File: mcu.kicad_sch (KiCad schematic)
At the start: 15 parts, among them U1 RP2040, U2 W25Q128JVS, Y1 Crystal_GND24

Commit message: add 3d models and do other stuff
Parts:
- added R8, R9: 5.1k, Resistor_SMD:R_0402_1005Metric, symbol Device:R_Small
- C1, C2: footprint (none) -> Capacitor_SMD:C_0402_1005Metric
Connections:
- net +3V3: now also R8.2, R9.2
- net MOSI: now reaches U1.12 (GPIO9)
- net MISO: now reaches U1.13 (GPIO10)
- net SCK: now reaches U1.14 (GPIO11)
- net M_LED_D: now reaches U1.15 (GPIO12)
- net BARO_CS: now reaches U1.16 (GPIO13)
- net IMU_CS: now reaches U1.17 (GPIO14)
- net RADIO_CS: now reaches U1.2 (GPIO0)
- net M_S6: now reaches U1.27 (GPIO16)
- net M_S5: now reaches U1.28 (GPIO17)
- net RADIO_D0: now reaches U1.3 (GPIO1)
- net M_S4: now reaches U1.36 (GPIO24)
- net M_S3: now reaches U1.37 (GPIO25)
- net BATTERY_SENSE: now reaches U1.38 (GPIO26_ADC0)
- net RADIO_RESET: now reaches U1.4 (GPIO2)
- net M_S1: now reaches U1.40 (GPIO28_ADC2)
- net M_S2: now reaches U1.41 (GPIO29_ADC3)
- net SDA: now reaches U1.6 (GPIO4)
- net SDA: now also R8.1
- net SCL: now reaches U1.7 (GPIO5)
- net SCL: now also R9.1
- net ARM_SWITCH: now reaches U1.8 (GPIO6)

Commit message: add some TVS diodes
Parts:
- added C25: 100n, Capacitor_SMD:C_0402_1005Metric, symbol Device:C_Small
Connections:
- net +3V3: now also U2.8 (VCC), C25.1
- net GND: now also C25.2
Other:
- moved on the sheet: U2

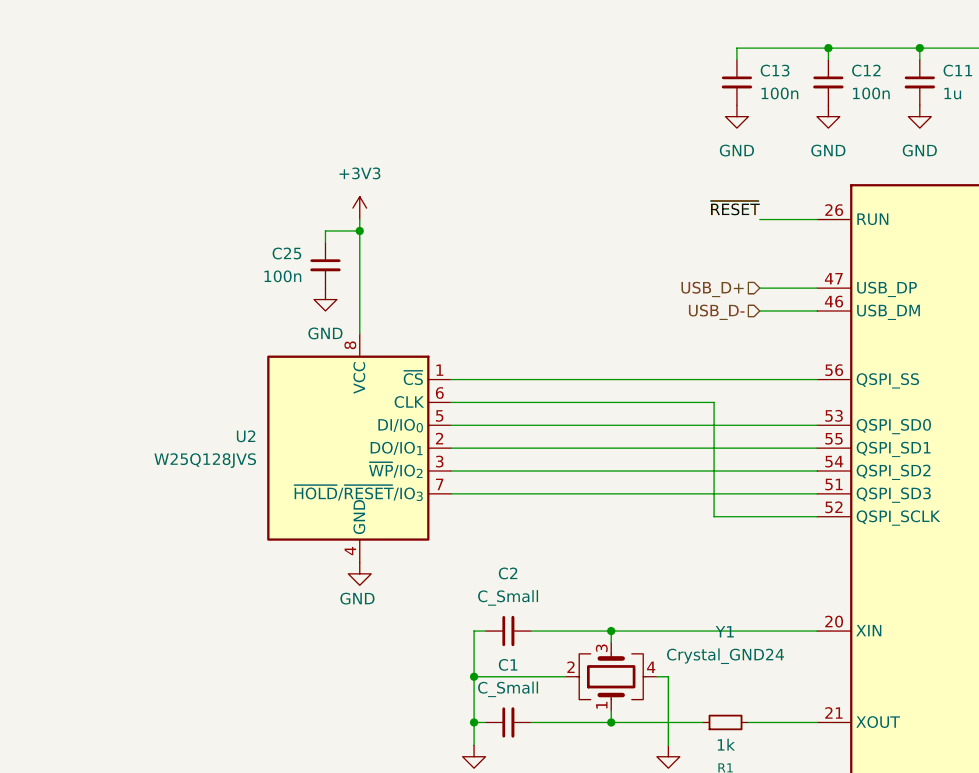
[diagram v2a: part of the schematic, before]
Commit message: update schematics and add 3d models
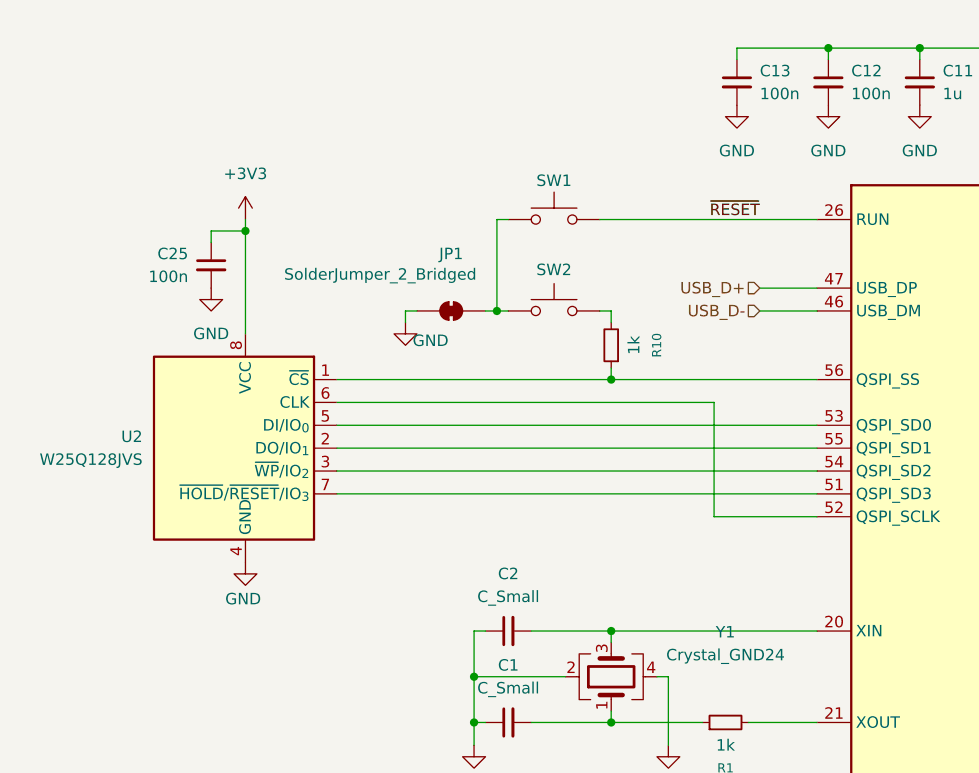
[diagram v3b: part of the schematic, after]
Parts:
- added JP1: SolderJumper_2_Bridged, Jumper:SolderJumper-2_P1.3mm_Bridged_RoundedPad1.0x1.5mm, symbol Jumper:SolderJumper_2_Bridged
- added R10: 1k, Resistor_SMD:R_0402_1005Metric, symbol Device:R_Small
- added SW1, SW2: SW_Push, beavs-footprints:SW_SPST_TS-1088-AR02016, symbol Switch:SW_Push
- C10, C12, C13, C14, C25, C7, C8, C9: LCSC (none) -> C1525
- C11, C6: LCSC (none) -> C52923
- R1: LCSC (none) -> C11702
- R8, R9: LCSC (none) -> C25905
- U1: LCSC (none) -> C2040
- U2: LCSC (none) -> C97521
- Y1: LCSC (none) -> C20625731
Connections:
- net GND: now also JP1.1 (A)
- net ~{RESET}: now also SW1.2
- net at U1.56 (QSPI_SS), U2.1 (~{CS}): now also R10.1
- new net: JP1.2 (B), SW1.1, SW2.1
- new net: R10.2, SW2.2
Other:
- moved on the sheet: C25, U2

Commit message: change out LEDs, add silk, start getting ready for fab
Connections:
- net GPIO_EXTINT: now reaches U1.39 (GPIO27_ADC1)
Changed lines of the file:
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@@
+	(wire
+		(pts
+			(xy 193.04 115.57) (xy 198.12 115.57)
+		)
+		(stroke
+			(width 0)
+			(type default)
+		)
+	)
 	(wire
 		(pts
@@
 		(effects
 			(font
+				(size 1.27 1.27)
+			)
+			(justify left)
+		)
+	)
+	(hierarchical_label "GPIO_EXTINT"
+		(shape output)
+		(at 198.12 115.57 0)
+		(effects
+			(font

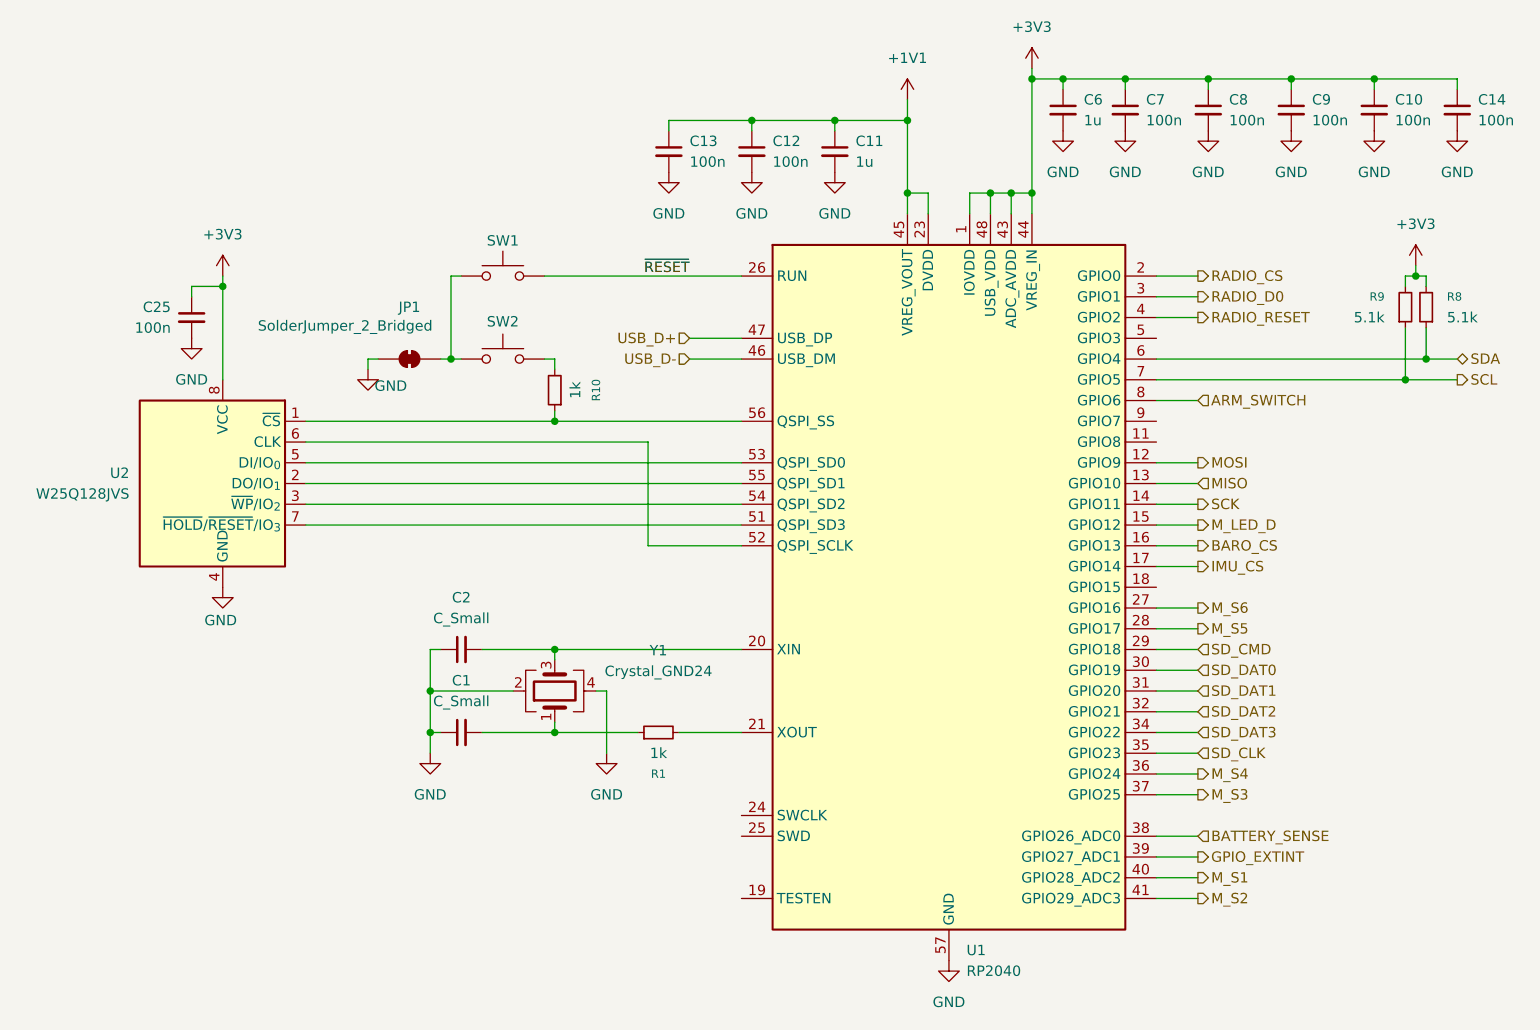
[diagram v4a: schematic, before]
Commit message: stapling vias, silk, minor schematic tweaks
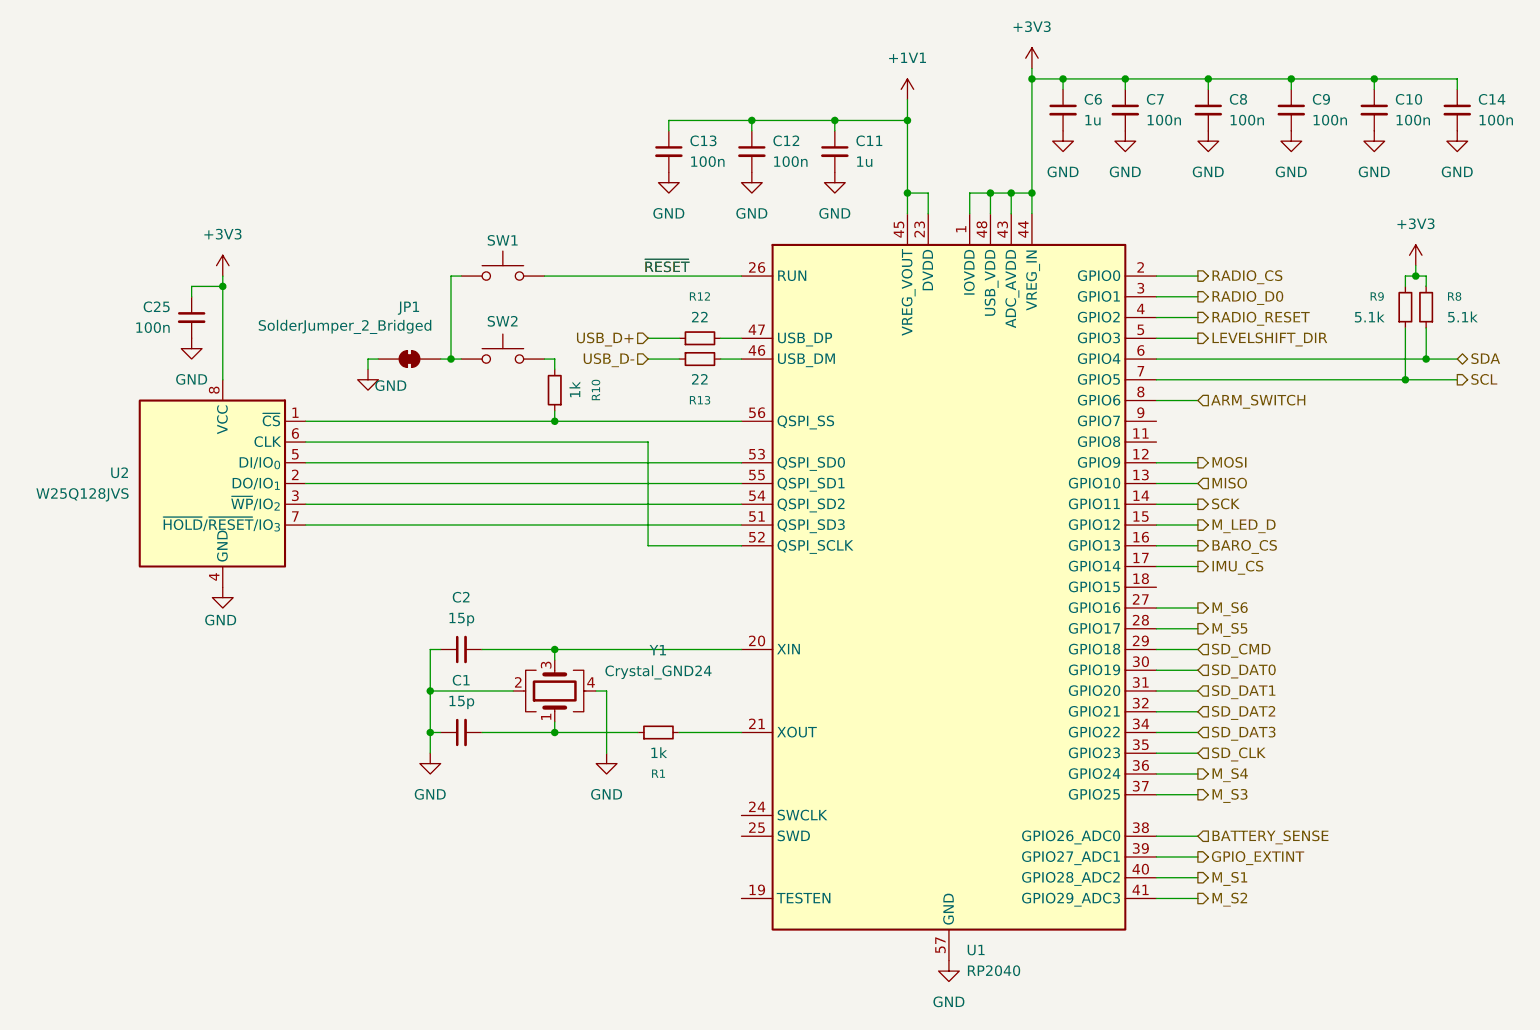
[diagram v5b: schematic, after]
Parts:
- added R12, R13: 22, Resistor_SMD:R_0402_1005Metric, symbol Device:R_Small
- C1, C2: value C_Small -> 15p; LCSC (none) -> C1548
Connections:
- net USB_D+: now also R12.1; no longer U1.47 (USB_DP)
- net USB_D-: now also R13.1; no longer U1.46 (USB_DM)
- net LEVELSHIFT_DIR: now reaches U1.5 (GPIO3)
- new net: R13.2, U1.46 (USB_DM)
- new net: R12.2, U1.47 (USB_DP)
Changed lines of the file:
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@@
+	(wire
+		(pts
+			(xy 130.81 54.61) (xy 134.62 54.61)
+		)
+		(stroke
+			(width 0)
+			(type default)
+		)
+	)
 	(wire
 		(pts
@@
 	(wire
 		(pts
+			(xy 130.81 52.07) (xy 134.62 52.07)
+		)
+		(stroke
+			(width 0)
+			(type default)
+		)
+	)
+	(wire
+		(pts
 			(xy 177.8 20.32) (xy 177.8 34.29)
 		)
@@
 	(wire
 		(pts
+			(xy 139.7 52.07) (xy 142.24 52.07)
+		)
+		(stroke
+			(width 0)
+			(type default)
+		)
+	)
+	(wire
+		(pts
+			(xy 193.04 52.07) (xy 198.12 52.07)
+		)
+		(stroke
+			(width 0)
+			(type default)
+		)
+	)
+	(wire
+		(pts
 			(xy 104.14 90.17) (xy 104.14 95.25)
 		)
@@
 	(wire
 		(pts
-			(xy 135.89 52.07) (xy 142.24 52.07)
-		)
-		(stroke
-			(width 0)
-			(type default)
-		)
-	)
-	(wire
-		(pts
 			(xy 107.95 44.45) (xy 106.68 44.45)
 		)
@@
 	(wire
 		(pts
+			(xy 139.7 54.61) (xy 142.24 54.61)
+		)
+		(stroke
+			(width 0)
+			(type default)
+		)
+	)
+	(wire
+		(pts
 			(xy 119.38 100.33) (xy 119.38 99.06)
 		)
@@
 		(pts
 			(xy 223.52 57.15) (xy 229.87 57.15)
-		)
-		(stroke
-			(width 0)
-			(type default)
-		)
-	)
-	(wire
-		(pts
-			(xy 135.89 54.61) (xy 142.24 54.61)
 		)
 		(stroke
@@
 	(hierarchical_label "USB_D+"
 		(shape input)
-		(at 135.89 52.07 180)
+		(at 130.81 52.07 180)
 		(effects
 			(font
@@
 		)
 	)
+	(hierarchical_label "LEVELSHIFT_DIR"
+		(shape output)
+		(at 198.12 52.07 0)
+		(effects
+			(font
+				(size 1.27 1.27)
+			)
+			(justify left)
+		)
+	)
 	(hierarchical_label "SD_CLK"
 		(shape input)
@@
 	(hierarchical_label "USB_D-"
 		(shape input)
-		(at 135.89 54.61 180)
+		(at 130.81 54.61 180)
 		(effects
 			(font
@@
 			)
 		)
-		(property "Value" "C_Small"
+		(property "Value" "15p"
 			(at 107.9563 86.36 90)
 			(effects
@@
 			)
 		)
-		(property "LCSC" ""
+		(property "LCSC" "C1548"
 			(at 107.95 90.17 90)
 			(effects
@@
 				(path "/49232f62-a438-4b3e-9be5-c2b3074d8de1/41e54b18-0bb2-4af3-8e30-a27cf4650be3"
 					(reference "#PWR076")
+					(unit 1)
+				)
+			)
+		)
+	)
+	(symbol
+		(lib_id "Device:R_Small")
+		(at 137.16 54.61 90)
+		(mirror x)
+		(unit 1)
+		(exclude_from_sim no)
+		(in_bom yes)
+		(on_board yes)
+		(dnp no)
+		(property "Reference" "R13"
+			(at 137.16 59.69 90)
+			(effects
+				(font
+					(size 1.016 1.016)
+				)
+			)
+		)
+		(property "Value" "22"
+			(at 137.16 57.15 90)
+			(effects
+				(font
+					(size 1.27 1.27)
+				)
+			)
+		)
+		(property "Footprint" "Resistor_SMD:R_0402_1005Metric"
+			(at 137.16 54.61 0)
+			(effects
+				(font
+					(size 1.27 1.27)
+				)
+				(hide yes)
+			)
+		)
+		(property "Datasheet" "~"
+			(at 137.16 54.61 0)
+			(effects
+				(font
+					(size 1.27 1.27)
+				)
+				(hide yes)
+			)
+		)
+		(property "Description" "Resistor, small symbol"
+			(at 137.16 54.61 0)
+			(effects
+				(font
+					(size 1.27 1.27)
+				)
+				(hide yes)
+			)
+		)
+		(property "LCSC" "C25092"
+			(at 137.16 54.61 90)
+			(effects
+				(font
+					(size 1.27 1.27)
+				)
+				(hide yes)
+			)
+		)
+		(pin "2"
+		)
+		(pin "1"
+		)
+		(instances
+			(project "beavs-sketch-0"
+				(path "/49232f62-a438-4b3e-9be5-c2b3074d8de1/41e54b18-0bb2-4af3-8e30-a27cf4650be3"
+					(reference "R13")
 					(unit 1)
 				)
@@
 	)
 	(symbol
+		(lib_id "Device:R_Small")
+		(at 137.16 52.07 90)
+		(unit 1)
+		(exclude_from_sim no)
+		(in_bom yes)
+		(on_board yes)
+		(dnp no)
+		(fields_autoplaced yes)
+		(property "Reference" "R12"
+			(at 137.16 46.99 90)
+			(effects
+				(font
+					(size 1.016 1.016)
+				)
+			)
+		)
+		(property "Value" "22"
+			(at 137.16 49.53 90)
+			(effects
+				(font
+					(size 1.27 1.27)
+				)
+			)
+		)
+		(property "Footprint" "Resistor_SMD:R_0402_1005Metric"
+			(at 137.16 52.07 0)
+			(effects
+				(font
+					(size 1.27 1.27)
+				)
+				(hide yes)
+			)
+		)
+		(property "Datasheet" "~"
+			(at 137.16 52.07 0)
+			(effects
+				(font
+					(size 1.27 1.27)
+				)
+				(hide yes)
+			)
+		)
+		(property "Description" "Resistor, small symbol"
+			(at 137.16 52.07 0)
+			(effects
+				(font
+					(size 1.27 1.27)
+				)
+				(hide yes)
+			)
+		)
+		(property "LCSC" "C25092"
+			(at 137.16 52.07 90)
+			(effects
+				(font
+					(size 1.27 1.27)
+				)
+				(hide yes)
+			)
+		)
+		(pin "2"
+		)
+		(pin "1"
+		)
+		(instances
+			(project ""
+				(path "/49232f62-a438-4b3e-9be5-c2b3074d8de1/41e54b18-0bb2-4af3-8e30-a27cf4650be3"
+					(reference "R12")
+					(unit 1)
+				)
+			)
+		)
+	)
+	(symbol
 		(lib_id "Device:Crystal_GND24")
 		(at 119.38 95.25 90)
@@
 			)
 		)
-		(property "Value" "C_Small"
+		(property "Value" "15p"
 			(at 107.9563 96.52 90)
 			(effects
@@
 			)
 		)
-		(property "LCSC" ""
+		(property "LCSC" "C1548"
 			(at 107.95 100.33 90)
 			(effects

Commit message: I may be stupid
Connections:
- net SERVO_POWER_EN: now reaches U1.11 (GPIO8)
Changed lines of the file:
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@@
+	(wire
+		(pts
+			(xy 193.04 64.77) (xy 198.12 64.77)
+		)
+		(stroke
+			(width 0)
+			(type default)
+		)
+	)
 	(wire
 		(pts
@@
 		(effects
 			(font
+				(size 1.27 1.27)
+			)
+			(justify left)
+		)
+	)
+	(hierarchical_label "SERVO_POWER_EN"
+		(shape output)
+		(at 198.12 64.77 0)
+		(effects
+			(font

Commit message: bigger pours for FETs, various cleanup, switching to different level shifter
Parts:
- R12, R13: LCSC C25092 -> C25079
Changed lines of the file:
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@@
 			)
 		)
+		(property "digikey" ""
+			(at 219.71 24.13 0)
+			(effects
+				(font
+					(size 1.27 1.27)
+				)
+				(hide yes)
+			)
+		)
 		(pin "1"
 		)
@@
 			)
 		)
+		(property "digikey" ""
+			(at 226.06 48.26 0)
+			(effects
+				(font
+					(size 1.27 1.27)
+				)
+				(hide yes)
+			)
+		)
 		(pin "2"
 		)
@@
 			)
 		)
+		(property "digikey" ""
+			(at 107.95 90.17 90)
+			(effects
+				(font
+					(size 1.27 1.27)
+				)
+				(hide yes)
+			)
+		)
 		(pin "1"
 		)
@@
 			)
 		)
+		(property "digikey" ""
+			(at 113.03 54.61 0)
+			(effects
+				(font
+					(size 1.27 1.27)
+				)
+				(hide yes)
+			)
+		)
 		(pin "2"
 		)
@@
 			)
 		)
-		(property "LCSC" "C25092"
+		(property "LCSC" "C25079"
+			(at 137.16 54.61 90)
+			(effects
+				(font
+					(size 1.27 1.27)
+				)
+				(hide yes)
+			)
+		)
+		(property "digikey" ""
 			(at 137.16 54.61 90)
 			(effects
@@
 			)
 		)
+		(property "digikey" ""
+			(at 189.23 24.13 0)
+			(effects
+				(font
+					(size 1.27 1.27)
+				)
+				(hide yes)
+			)
+		)
 		(pin "1"
 		)
@@
 			)
 		)
+		(property "digikey" ""
+			(at 74.93 49.53 0)
+			(effects
+				(font
+					(size 1.27 1.27)
+				)
+				(hide yes)
+			)
+		)
 		(pin "1"
 		)
@@
 			)
 		)
+		(property "digikey" ""
+			(at 209.55 24.13 0)
+			(effects
+				(font
+					(size 1.27 1.27)
+				)
+				(hide yes)
+			)
+		)
 		(pin "1"
 		)
@@
 			)
 		)
-		(property "LCSC" "C25092"
+		(property "LCSC" "C25079"
+			(at 137.16 52.07 90)
+			(effects
+				(font
+					(size 1.27 1.27)
+				)
+				(hide yes)
+			)
+		)
+		(property "digikey" ""
 			(at 137.16 52.07 90)
 			(effects
@@
 			)
 		)
+		(property "digikey" ""
+			(at 119.38 95.25 90)
+			(effects
+				(font
+					(size 1.27 1.27)
+				)
+				(hide yes)
+			)
+		)
 		(pin "2"
 		)
@@
 			)
 		)
+		(property "digikey" ""
+			(at 223.52 48.26 0)
+			(effects
+				(font
+					(size 1.27 1.27)
+				)
+				(hide yes)
+			)
+		)
 		(pin "2"
 		)
@@
 			)
 		)
+		(property "digikey" ""
+			(at 133.35 29.21 0)
+			(effects
+				(font
+					(size 1.27 1.27)
+				)
+				(hide yes)
+			)
+		)
 		(pin "1"
 		)
@@
 			)
 		)
+		(property "digikey" ""
+			(at 101.6 54.61 0)
+			(effects
+				(font
+					(size 1.27 1.27)
+				)
+				(hide yes)
+			)
+		)
 		(pin "2"
 		)
@@
 			)
 		)
+		(property "digikey" ""
+			(at 153.67 29.21 0)
+			(effects
+				(font
+					(size 1.27 1.27)
+				)
+				(hide yes)
+			)
+		)
 		(pin "1"
 		)
@@
 			)
 		)
+		(property "digikey" ""
+			(at 107.95 100.33 90)
+			(effects
+				(font
+					(size 1.27 1.27)
+				)
+				(hide yes)
+			)
+		)
 		(pin "1"
 		)
@@
 			)
 		)
+		(property "digikey" ""
+			(at 143.51 29.21 0)
+			(effects
+				(font
+					(size 1.27 1.27)
+				)
+				(hide yes)
+			)
+		)
 		(pin "1"
 		)
@@
 			)
 		)
+		(property "digikey" ""
+			(at 78.74 69.85 0)
+			(effects
+				(font
+					(size 1.27 1.27)
+				)
+				(hide yes)
+			)
+		)
 		(pin "8"
 		)
@@
 			)
 		)
+		(property "digikey" ""
+			(at 181.61 24.13 0)
+			(effects
+				(font
+					(size 1.27 1.27)
+				)
+				(hide yes)
+			)
+		)
 		(pin "1"
 		)
@@
 			)
 		)
+		(property "digikey" ""
+			(at 199.39 24.13 0)
+			(effects
+				(font
+					(size 1.27 1.27)
+				)
+				(hide yes)
+			)
+		)
 		(pin "1"
 		)
@@
 			)
 		)
+		(property "digikey" ""
+			(at 113.03 44.45 0)
+			(effects
+				(font
+					(size 1.27 1.27)
+				)
+				(hide yes)
+			)
+		)
 		(pin "2"
 		)
@@
 			)
 		)
+		(property "digikey" ""
+			(at 229.87 24.13 0)
+			(effects
+				(font
+					(size 1.27 1.27)
+				)
+				(hide yes)
+			)
+		)
 		(pin "1"
 		)
@@
 			)
 		)
+		(property "digikey" ""
+			(at 119.38 58.42 90)
+			(effects
+				(font
+					(size 1.27 1.27)
+				)
+				(hide yes)
+			)
+		)
 		(pin "1"
 		)
@@
 			)
 		)
+		(property "digikey" ""
+			(at 132.08 100.33 90)
+			(effects
+				(font
+					(size 1.27 1.27)
+				)
+				(hide yes)
+			)
+		)
 		(pin "1"
 		)
@@
 			(at 167.64 82.55 0)
 			(effects
+				(font
+					(size 1.27 1.27)
+				)
+				(hide yes)
+			)
+		)
+		(property "digikey" ""
+			(at 167.64 82.55 0)
+			(effects

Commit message: changes apparently but idk what
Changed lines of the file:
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@@
 	)
 	(hierarchical_label "USB_D+"
-		(shape input)
+		(shape bidirectional)
 		(at 130.81 52.07 180)
 		(effects
@@
 	)
 	(hierarchical_label "USB_D-"
-		(shape input)
+		(shape bidirectional)
 		(at 130.81 54.61 180)
 		(effects
